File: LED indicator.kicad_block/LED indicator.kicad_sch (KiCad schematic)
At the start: 2 parts

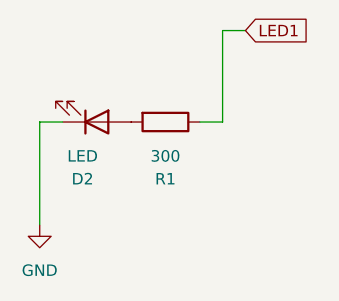
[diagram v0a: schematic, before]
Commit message: resstor footprint (I think!) and the net label for leds
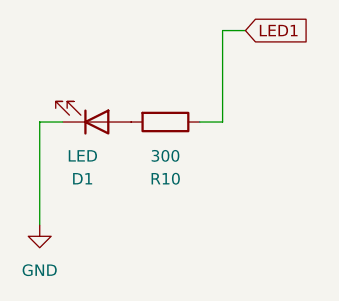
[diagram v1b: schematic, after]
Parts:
- R10: renamed from R1; footprint (none) -> Resistor_THT:R_Axial_DIN0207_L6.3mm_D2.5mm_P10.16mm_Horizontal
- renumbered D2 to D1
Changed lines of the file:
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@@
 		(in_pos_files yes)
 		(dnp no)
-		(property "Reference" "D2"
+		(property "Reference" "D1"
 			(at 223.2025 99.06 0)
 			(show_name no)
@@
 			(project "kicad-mobiflight-device-blocks-worksheet"
 				(path "/4714e232-3dfb-45f4-a0c3-3539b78f5138"
-					(reference "D2")
+					(reference "D1")
 					(unit 1)
 				)
@@
 		(in_pos_files yes)
 		(dnp no)
-		(property "Reference" "R1"
+		(property "Reference" "R10"
 			(at 232.41 99.06 90)
 			(show_name no)
@@
 			)
 		)
-		(property "Footprint" ""
+		(property "Footprint" "Resistor_THT:R_Axial_DIN0207_L6.3mm_D2.5mm_P10.16mm_Horizontal"
 			(at 232.41 90.932 90)
 			(hide yes)
@@
 			(project "kicad-mobiflight-device-blocks-worksheet"
 				(path "/4714e232-3dfb-45f4-a0c3-3539b78f5138"
-					(reference "R1")
+					(reference "R10")
 					(unit 1)
 				)
